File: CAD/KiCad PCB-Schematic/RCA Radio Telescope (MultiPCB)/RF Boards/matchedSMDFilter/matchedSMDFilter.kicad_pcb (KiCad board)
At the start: 2 copper layers, 0 parts

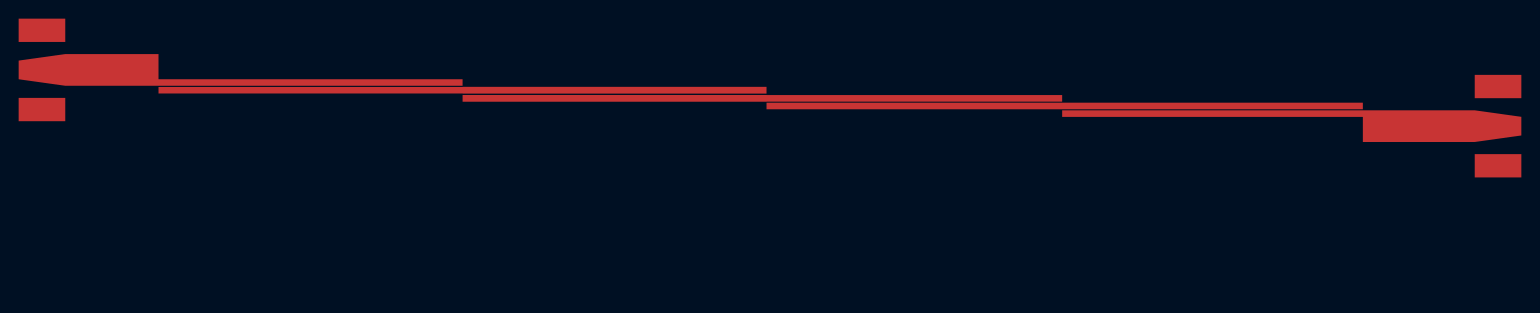
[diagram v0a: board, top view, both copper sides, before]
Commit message: RF Boards Redo (WIP)
- Overhauling current RF boards to keep 4 RF boards in total
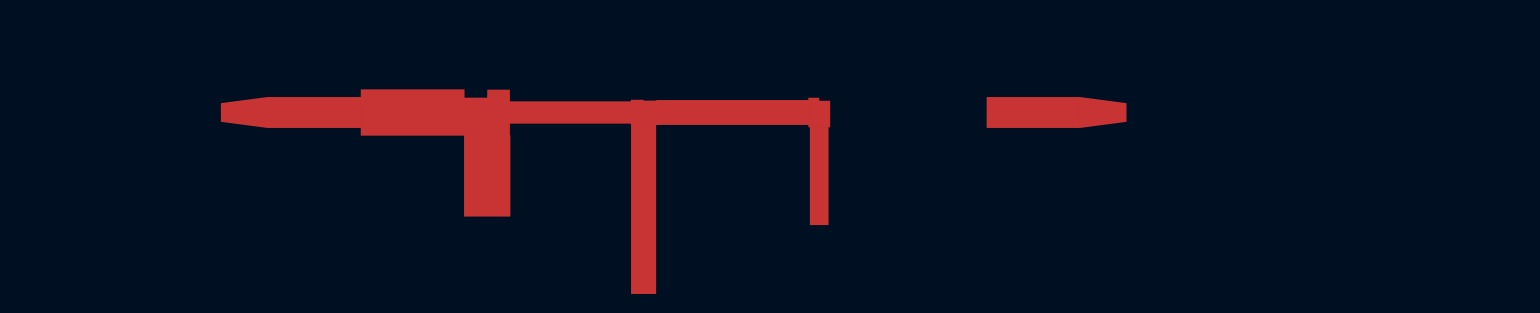
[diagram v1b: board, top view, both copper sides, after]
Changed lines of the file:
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@@
 	(gr_poly
 		(pts
-			(xy 152.75216 60) (xy 185 60) (xy 185 62.68986) (xy 196.99896 62.68986) (xy 201.99768 61.99136) (xy 201.99768 59.98984)
-			(xy 196.99896 59.29134) (xy 152.75216 59.29134)
+			(xy 125.52736 57.94122) (xy 125.52736 61.11114) (xy 127.87178 61.11114) (xy 127.87178 58.26888) (xy 126.6983 58.26888)
+			(xy 126.6983 57.94122)
 		)
 		(stroke
@@
 	(gr_poly
 		(pts
-			(xy 121.04534 57.65558) (xy 121.04534 57.64796) (xy 88.44952 57.64796) (xy 88.44952 58.37186) (xy 121.04534 58.37186)
-			(xy 121.04534 58.36424) (xy 152.75216 58.36424) (xy 152.75216 57.65558)
+			(xy 88.65672 57.93614) (xy 88.65672 61.9722) (xy 93.52336 61.9722) (xy 93.52336 57.08016) (xy 91.09004 57.08016)
+			(xy 91.09004 57.93614)
 		)
 		(stroke
@@
 	(gr_poly
 		(pts
-			(xy 121.04534 59.18212) (xy 152.75216 59.18212) (xy 185 59.18212) (xy 185 58.47346) (xy 152.75216 58.47346)
-			(xy 121.04534 58.47346)
+			(xy 77.53026 57.86839) (xy 67.53025 57.86839) (xy 67.53025 61.18398) (xy 77.53026 61.18398)
 		)
 		(stroke
@@
 	(gr_poly
 		(pts
-			(xy 55.83846 57.48794) (xy 88.44952 57.48794) (xy 88.44952 57.50064) (xy 121.04534 57.50064) (xy 121.04534 56.7742)
-			(xy 88.44952 56.7742) (xy 88.44952 56.7869) (xy 55.83846 56.7869)
+			(xy 106.49797 58.3313) (xy 93.52307 58.3313) (xy 93.52307 60.72106) (xy 106.49797 60.72106)
 		)
 		(stroke
@@
 	(gr_poly
 		(pts
-			(xy 45.83911 49.46122) (xy 40.83912 49.46122) (xy 40.83912 51.96122) (xy 45.83911 51.96122)
+			(xy 106.49768 58.1622) (xy 106.49768 60.89016) (xy 109.22818 60.89016) (xy 109.22818 58.25364) (xy 107.86166 58.25364)
+			(xy 107.86166 58.1622)
 		)
 		(stroke
@@
 	(gr_poly
 		(pts
-			(xy 55.83846 55.95886) (xy 55.83846 53.26138) (xy 45.84102 53.26138) (xy 40.83976 53.95988) (xy 40.83976 55.9614)
-			(xy 45.84102 56.6599) (xy 88.44952 56.6599) (xy 88.44952 55.95886)
+			(xy 67.53154 61.1848) (xy 67.53154 57.86756) (xy 62.53028 58.52542) (xy 62.53028 60.52694)
 		)
 		(stroke
@@
 	(gr_poly
 		(pts
-			(xy 201.99831 63.99002) (xy 196.99832 63.99002) (xy 196.99832 66.49002) (xy 201.99831 66.49002)
+			(xy 125.52649 58.19069) (xy 109.2265 58.19069) (xy 109.2265 60.86168) (xy 125.52649 60.86168)
 		)
 		(stroke
@@
 	(gr_poly
 		(pts
-			(xy 201.99831 55.49118) (xy 196.99832 55.49118) (xy 196.99832 57.99118) (xy 201.99831 57.99118)
+			(xy 93.57448 61.97272) (xy 88.6056 61.97272) (xy 88.6056 70.68896) (xy 93.57448 70.68896)
 		)
 		(stroke
@@
 	(gr_poly
 		(pts
-			(xy 45.83911 57.96006) (xy 40.83912 57.96006) (xy 40.83912 60.46006) (xy 45.83911 60.46006)
+			(xy 154.65228 57.86839) (xy 144.65227 57.86839) (xy 144.65227 61.18398) (xy 154.65228 61.18398)
 		)
 		(stroke
+			(width 0)
+			(type solid)
+		)
+		(fill solid)
+		(layer "F.Cu")
+	)
+	(gr_poly
+		(pts
+			(xy 109.2072 60.89128) (xy 106.51612 60.89128) (xy 106.51612 78.98908) (xy 109.2072 78.98908)
+		)
+		(stroke
+			(width 0)
+			(type solid)
+		)
+		(fill solid)
+		(layer "F.Cu")
+	)
+	(gr_poly
+		(pts
+			(xy 154.65354 57.86756) (xy 154.65354 61.1848) (xy 159.65226 60.52694) (xy 159.65226 58.52542)
+		)
+		(stroke
+			(width 0)
+			(type solid)
+		)
+		(fill solid)
+		(layer "F.Cu")
+	)
+	(gr_poly
+		(pts
+			(xy 127.7 61.11249) (xy 125.6966 61.11249) (xy 125.6966 71.6) (xy 127.7 71.6)
+		)
+		(stroke
+			(width 0)
+			(type solid)
+		)
+		(fill solid)
+		(layer "F.Cu")
+	)
+	(gr_poly
+		(pts
+			(xy 88.65716 57.04357) (xy 77.53107 57.04357) (xy 77.53107 62.00879) (xy 88.65716 62.00879)
+		)
+		(stroke
